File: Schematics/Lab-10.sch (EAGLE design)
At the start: 15 parts, among them IC1 OP350N, Q1 IRLD024

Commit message: Modified changes after prep checkout
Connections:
- removed net N$3: C2.2, IC1.-VS, R6.1
- net +3V3: now also C2.2, IC1.-VS, R6.1
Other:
- note added: "Should be an RC Filter"
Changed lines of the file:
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@@
 <part name="R8" library="EE445L" deviceset="RESISTOR" device="0204/5"/>
 <part name="C2" library="EE445L" deviceset="CAPACITOR" device="025-024X044"/>
+<part name="+3V2" library="EE445L" deviceset="+3V3" device=""/>
 </parts>
 <sheets>
 <sheet>
 <plain>
+<text x="124.46" y="111.76" size="1.778" layer="91">Should be an RC Filter</text>
 </plain>
 <instances>
@@
 <attribute name="VALUE" x="201.549" y="141.224" size="1.778" layer="96" rot="R270"/>
 </instance>
+<instance part="+3V2" gate="G$1" x="205.74" y="154.94" smashed="yes">
+<attribute name="VALUE" x="203.2" y="149.86" size="1.778" layer="96" rot="R90"/>
+</instance>
 </instances>
 <busses>
@@
 <pinref part="+3V1" gate="G$1" pin="+3V3"/>
 </segment>
+<segment>
+<pinref part="IC1" gate="P" pin="-VS"/>
+<wire x1="198.12" y1="162.56" x2="198.12" y2="152.4" width="0.1524" layer="91"/>
+<pinref part="C2" gate="G$1" pin="2"/>
+<wire x1="198.12" y1="152.4" x2="198.12" y2="142.24" width="0.1524" layer="91"/>
+<wire x1="198.12" y1="142.24" x2="200.66" y2="142.24" width="0.1524" layer="91"/>
+<wire x1="198.12" y1="152.4" x2="162.56" y2="152.4" width="0.1524" layer="91"/>
+<junction x="198.12" y="152.4"/>
+<pinref part="R6" gate="G$1" pin="1"/>
+<wire x1="162.56" y1="152.4" x2="162.56" y2="154.94" width="0.1524" layer="91"/>
+<pinref part="+3V2" gate="G$1" pin="+3V3"/>
+<wire x1="198.12" y1="152.4" x2="205.74" y2="152.4" width="0.1524" layer="91"/>
+</segment>
 </net>
 <net name="M0_PWM0" class="0">
@@
 </segment>
 </net>
-<net name="N$3" class="0">
-<segment>
-<pinref part="IC1" gate="P" pin="-VS"/>
-<wire x1="198.12" y1="162.56" x2="198.12" y2="152.4" width="0.1524" layer="91"/>
-<pinref part="C2" gate="G$1" pin="2"/>
-<wire x1="198.12" y1="152.4" x2="198.12" y2="142.24" width="0.1524" layer="91"/>
-<wire x1="198.12" y1="142.24" x2="200.66" y2="142.24" width="0.1524" layer="91"/>
-<wire x1="198.12" y1="152.4" x2="162.56" y2="152.4" width="0.1524" layer="91"/>
-<junction x="198.12" y="152.4"/>
-<pinref part="R6" gate="G$1" pin="1"/>
-<wire x1="162.56" y1="152.4" x2="162.56" y2="154.94" width="0.1524" layer="91"/>
-</segment>
-</net>

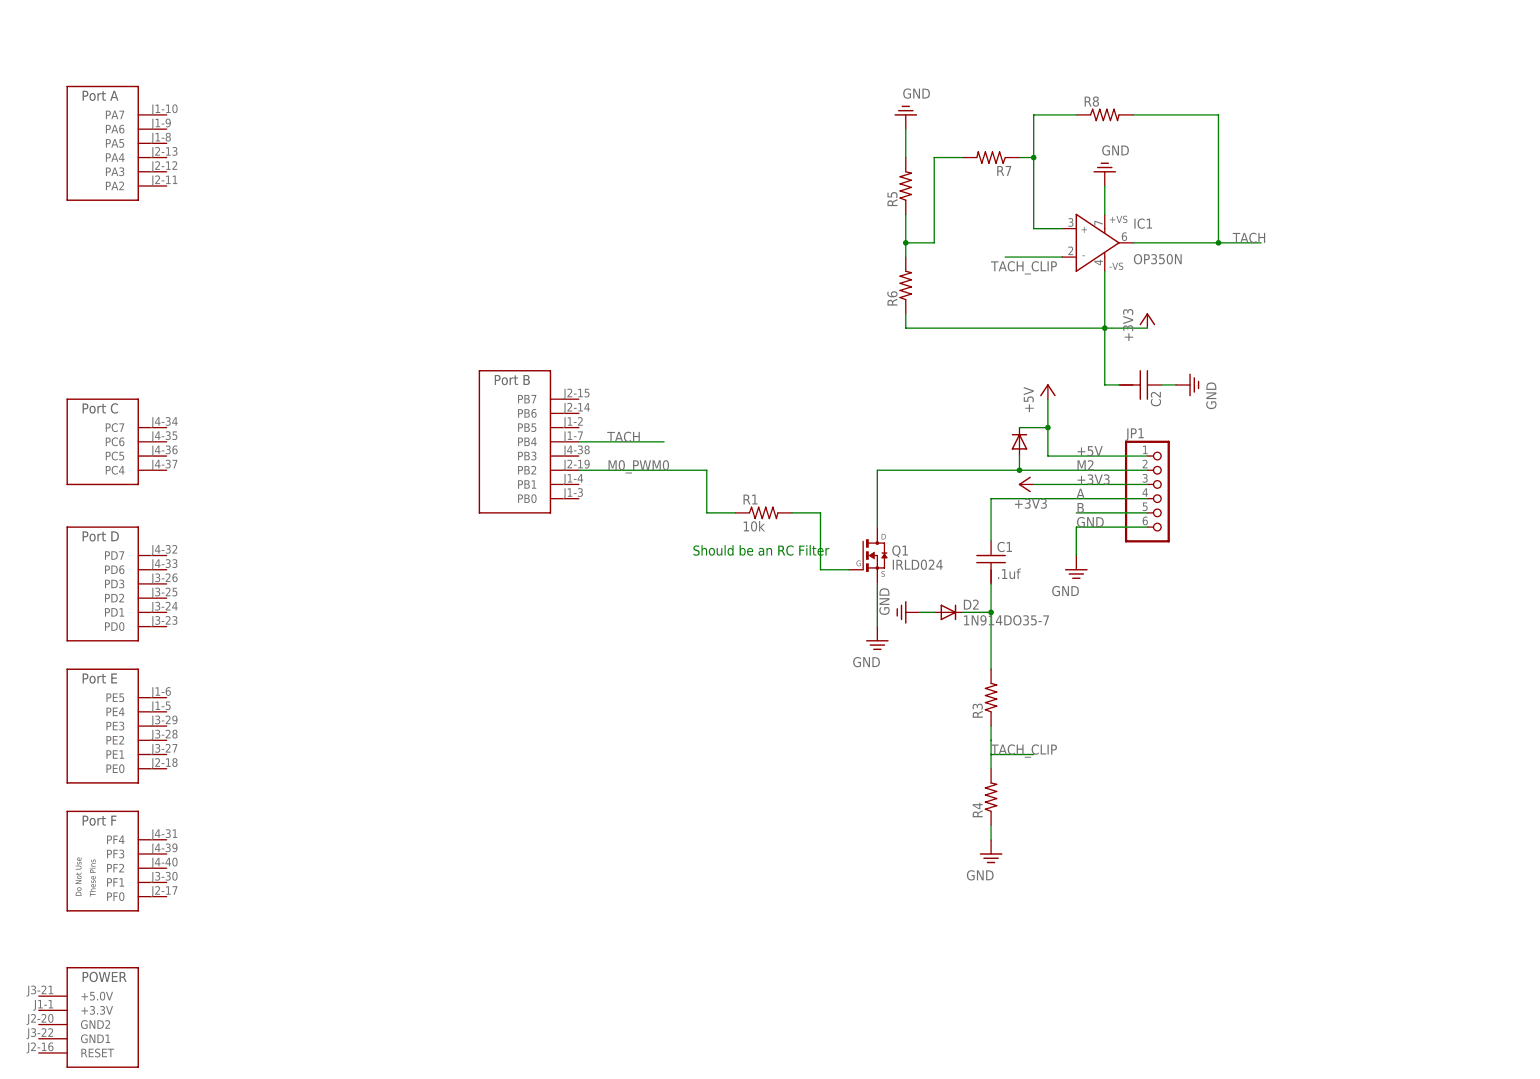
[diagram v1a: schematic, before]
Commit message: Added LCD interface to the schematic
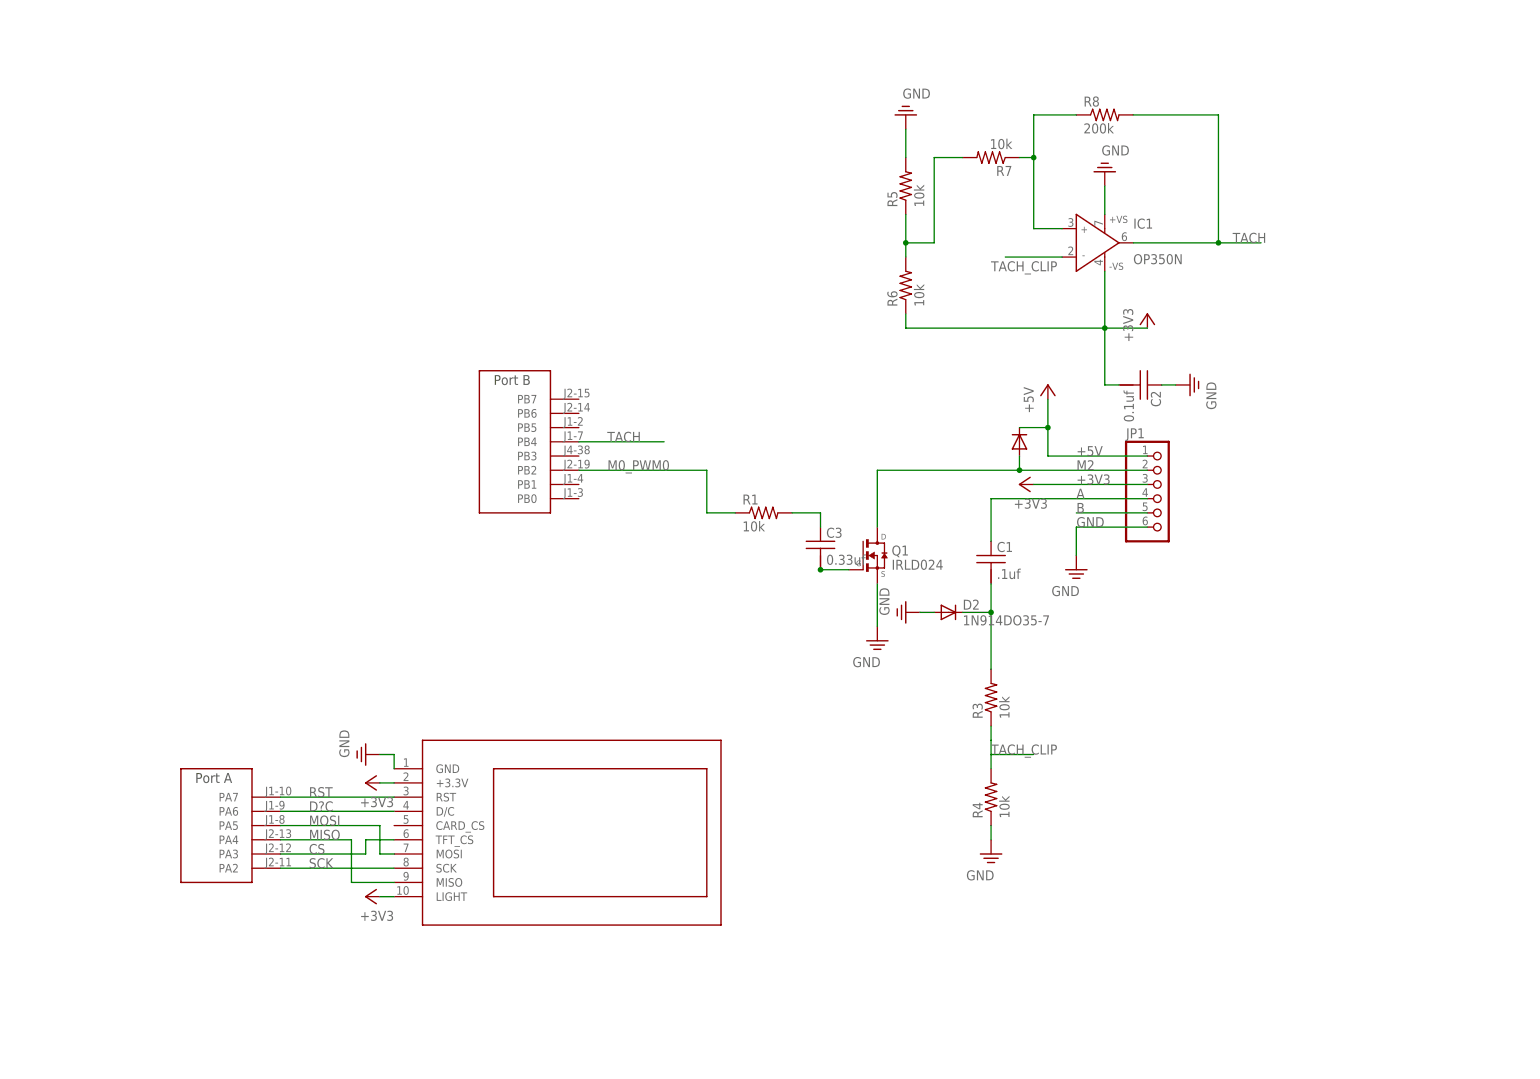
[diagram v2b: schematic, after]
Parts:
- added C3: 0.33uf, EE445L:CAPACITOR025-024X044
- added U$2: ST7735, EE445L:ST7735
- C2: value (none) -> 0.1uf
- R3, R4, R5, R6, R7: value (none) -> 10k
- R8: value (none) -> 200k
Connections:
- new net CS: U$1G$1.PA3, U$2.TFT_CS
- new net D?C: U$1G$1.PA6, U$2.D/C
- new net MISO: U$1G$1.PA4, U$2.MISO
- new net MOSI: U$1G$1.PA5, U$2.MOSI
- new net N$3: C3.2, Q1.G
- new net RST: U$1G$1.PA7, U$2.RST
- new net SCK: U$1G$1.PA2, U$2.SCK
- net +3V3: now also U$2.+3.3V, U$2.LIGHT
- net GND: now also U$2.GND
- net N$1: now also C3.1; no longer Q1.G
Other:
- note removed: "Should be an RC Filter"
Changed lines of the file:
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@@
 <part name="D2" library="EE445L" deviceset="1N914" device="DO35-7"/>
 <part name="SUPPLY3" library="EE445L" deviceset="GND" device=""/>
-<part name="R3" library="EE445L" deviceset="RESISTOR" device="0204/7"/>
-<part name="R4" library="EE445L" deviceset="RESISTOR" device="0204/7"/>
+<part name="R3" library="EE445L" deviceset="RESISTOR" device="0204/7" value="10k"/>
+<part name="R4" library="EE445L" deviceset="RESISTOR" device="0204/7" value="10k"/>
 <part name="SUPPLY4" library="EE445L" deviceset="GND" device=""/>
 <part name="IC1" library="EE445L" deviceset="OP350" device="N"/>
@@
 <part name="SUPPLY6" library="EE445L" deviceset="GND" device=""/>
 <part name="SUPPLY7" library="EE445L" deviceset="GND" device=""/>
-<part name="R5" library="EE445L" deviceset="RESISTOR" device="0204/5"/>
-<part name="R6" library="EE445L" deviceset="RESISTOR" device="0204/5"/>
-<part name="R7" library="EE445L" deviceset="RESISTOR" device="0204/5"/>
-<part name="R8" library="EE445L" deviceset="RESISTOR" device="0204/5"/>
-<part name="C2" library="EE445L" deviceset="CAPACITOR" device="025-024X044"/>
+<part name="R5" library="EE445L" deviceset="RESISTOR" device="0204/5" value="10k"/>
+<part name="R6" library="EE445L" deviceset="RESISTOR" device="0204/5" value="10k"/>
+<part name="R7" library="EE445L" deviceset="RESISTOR" device="0204/5" value="10k"/>
+<part name="R8" library="EE445L" deviceset="RESISTOR" device="0204/5" value="200k"/>
+<part name="C2" library="EE445L" deviceset="CAPACITOR" device="025-024X044" value="0.1uf"/>
 <part name="+3V2" library="EE445L" deviceset="+3V3" device=""/>
+<part name="C3" library="EE445L" deviceset="CAPACITOR" device="025-024X044" value="0.33uf"/>
+<part name="U$2" library="EE445L" deviceset="ST7735" device=""/>
+<part name="+3V3" library="EE445L" deviceset="+3V3" device=""/>
+<part name="+3V4" library="EE445L" deviceset="+3V3" device=""/>
+<part name="SUPPLY8" library="EE445L" deviceset="GND" device=""/>
 </parts>
 <sheets>
 <sheet>
 <plain>
-<text x="124.46" y="111.76" size="1.778" layer="91">Should be an RC Filter</text>
 </plain>
 <instances>
@@
 <attribute name="DRAWING_NAME" x="190.5" y="19.05" size="2.54" layer="94"/>
 </instance>
-<instance part="U$1" gate="G$1" x="12.7" y="175.26" smashed="yes"/>
+<instance part="U$1" gate="G$1" x="33.02" y="53.34" smashed="yes"/>
 <instance part="U$1" gate="G$2" x="86.36" y="119.38" smashed="yes"/>
-<instance part="U$1" gate="G$3" x="12.7" y="124.46" smashed="yes"/>
-<instance part="U$1" gate="G$4" x="12.7" y="96.52" smashed="yes"/>
-<instance part="U$1" gate="G$5" x="12.7" y="71.12" smashed="yes"/>
-<instance part="U$1" gate="G$6" x="12.7" y="48.26" smashed="yes"/>
-<instance part="U$1" gate="G$7" x="12.7" y="20.32" smashed="yes"/>
 <instance part="D2" gate="G$1" x="170.18" y="101.6" smashed="yes">
 <attribute name="NAME" x="172.72" y="102.0826" size="1.778" layer="95"/>
@@
 <instance part="+3V2" gate="G$1" x="205.74" y="154.94" smashed="yes">
 <attribute name="VALUE" x="203.2" y="149.86" size="1.778" layer="96" rot="R90"/>
+</instance>
+<instance part="C3" gate="G$1" x="147.32" y="114.3" smashed="yes">
+<attribute name="NAME" x="148.336" y="114.935" size="1.778" layer="95"/>
+<attribute name="VALUE" x="148.336" y="110.109" size="1.778" layer="96"/>
+</instance>
+<instance part="U$2" gate="G$1" x="76.2" y="45.72" smashed="yes"/>
+<instance part="+3V3" gate="G$1" x="66.04" y="71.12" smashed="yes" rot="R90">
+<attribute name="VALUE" x="71.12" y="68.58" size="1.778" layer="96" rot="R180"/>
+</instance>
+<instance part="+3V4" gate="G$1" x="66.04" y="50.8" smashed="yes" rot="R90">
+<attribute name="VALUE" x="71.12" y="48.26" size="1.778" layer="96" rot="R180"/>
+</instance>
+<instance part="SUPPLY8" gate="GND" x="66.04" y="76.2" smashed="yes" rot="R270">
+<attribute name="VALUE" x="61.341" y="80.645" size="1.778" layer="96" rot="R270"/>
 </instance>
 </instances>
@@
 <pinref part="SUPPLY7" gate="GND" pin="GND"/>
 <wire x1="162.56" y1="182.88" x2="162.56" y2="187.96" width="0.1524" layer="91"/>
+</segment>
+<segment>
+<pinref part="SUPPLY8" gate="GND" pin="GND"/>
+<pinref part="U$2" gate="G$1" pin="GND"/>
+<wire x1="68.58" y1="76.2" x2="71.12" y2="76.2" width="0.1524" layer="91"/>
+<wire x1="71.12" y1="76.2" x2="71.12" y2="73.66" width="0.1524" layer="91"/>
 </segment>
 </net>
@@
 <wire x1="198.12" y1="152.4" x2="205.74" y2="152.4" width="0.1524" layer="91"/>
 </segment>
+<segment>
+<pinref part="+3V3" gate="G$1" pin="+3V3"/>
+<pinref part="U$2" gate="G$1" pin="+3.3V"/>
+<wire x1="68.58" y1="71.12" x2="71.12" y2="71.12" width="0.1524" layer="91"/>
+</segment>
+<segment>
+<pinref part="U$2" gate="G$1" pin="LIGHT"/>
+<pinref part="+3V4" gate="G$1" pin="+3V3"/>
+<wire x1="71.12" y1="50.8" x2="68.58" y2="50.8" width="0.1524" layer="91"/>
+</segment>
 </net>
 <net name="M0_PWM0" class="0">
@@
 <pinref part="R1" gate="G$1" pin="2"/>
 <wire x1="142.24" y1="119.38" x2="147.32" y2="119.38" width="0.1524" layer="91"/>
-<wire x1="147.32" y1="119.38" x2="147.32" y2="109.22" width="0.1524" layer="91"/>
-<pinref part="Q1" gate="G$1" pin="G"/>
-<wire x1="147.32" y1="109.22" x2="152.4" y2="109.22" width="0.1524" layer="91"/>
+<pinref part="C3" gate="G$1" pin="1"/>
+<wire x1="147.32" y1="119.38" x2="147.32" y2="116.84" width="0.1524" layer="91"/>
 </segment>
 </net>
@@
 </segment>
 </net>
+<net name="N$3" class="0">
+<segment>
+<pinref part="Q1" gate="G$1" pin="G"/>
+<pinref part="C3" gate="G$1" pin="2"/>
+<junction x="147.32" y="109.22"/>
+<wire x1="147.32" y1="109.22" x2="152.4" y2="109.22" width="0.1524" layer="91"/>
+</segment>
+</net>
+<net name="RST" class="0">
+<segment>
+<pinref part="U$1" gate="G$1" pin="PA7"/>
+<pinref part="U$2" gate="G$1" pin="RST"/>
+<wire x1="50.8" y1="68.58" x2="71.12" y2="68.58" width="0.1524" layer="91"/>
+<label x="55.88" y="68.58" size="1.778" layer="95"/>
+</segment>
+</net>
+<net name="D?C" class="0">
+<segment>
+<pinref part="U$1" gate="G$1" pin="PA6"/>
+<pinref part="U$2" gate="G$1" pin="D/C"/>
+<wire x1="50.8" y1="66.04" x2="71.12" y2="66.04" width="0.1524" layer="91"/>
+<label x="55.88" y="66.04" size="1.778" layer="95"/>
+</segment>
+</net>
+<net name="MOSI" class="0">
+<segment>
+<pinref part="U$1" gate="G$1" pin="PA5"/>
+<wire x1="50.8" y1="63.5" x2="68.58" y2="63.5" width="0.1524" layer="91"/>
+<pinref part="U$2" gate="G$1" pin="MOSI"/>
+<wire x1="68.58" y1="63.5" x2="68.58" y2="58.42" width="0.1524" layer="91"/>
+<wire x1="68.58" y1="58.42" x2="71.12" y2="58.42" width="0.1524" layer="91"/>
+<label x="55.88" y="63.5" size="1.778" layer="95"/>
+</segment>
+</net>
+<net name="MISO" class="0">
+<segment>
+<pinref part="U$1" gate="G$1" pin="PA4"/>
+<wire x1="50.8" y1="60.96" x2="63.5" y2="60.96" width="0.1524" layer="91"/>
+<pinref part="U$2" gate="G$1" pin="MISO"/>
+<wire x1="63.5" y1="60.96" x2="63.5" y2="53.34" width="0.1524" layer="91"/>
+<wire x1="63.5" y1="53.34" x2="71.12" y2="53.34" width="0.1524" layer="91"/>
+<label x="55.88" y="60.96" size="1.778" layer="95"/>
+</segment>
+</net>
+<net name="CS" class="0">
+<segment>
+<pinref part="U$1" gate="G$1" pin="PA3"/>
+<wire x1="50.8" y1="58.42" x2="66.04" y2="58.42" width="0.1524" layer="91"/>
+<pinref part="U$2" gate="G$1" pin="TFT_CS"/>
+<wire x1="66.04" y1="58.42" x2="66.04" y2="60.96" width="0.1524" layer="91"/>
+<wire x1="66.04" y1="60.96" x2="71.12" y2="60.96" width="0.1524" layer="91"/>
+<label x="55.88" y="58.42" size="1.778" layer="95"/>
+</segment>
+</net>
+<net name="SCK" class="0">
+<segment>
+<pinref part="U$1" gate="G$1" pin="PA2"/>
+<pinref part="U$2" gate="G$1" pin="SCK"/>
+<wire x1="50.8" y1="55.88" x2="71.12" y2="55.88" width="0.1524" layer="91"/>
+<label x="55.88" y="55.88" size="1.778" layer="95"/>
+</segment>
+</net>

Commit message: Added wifi block
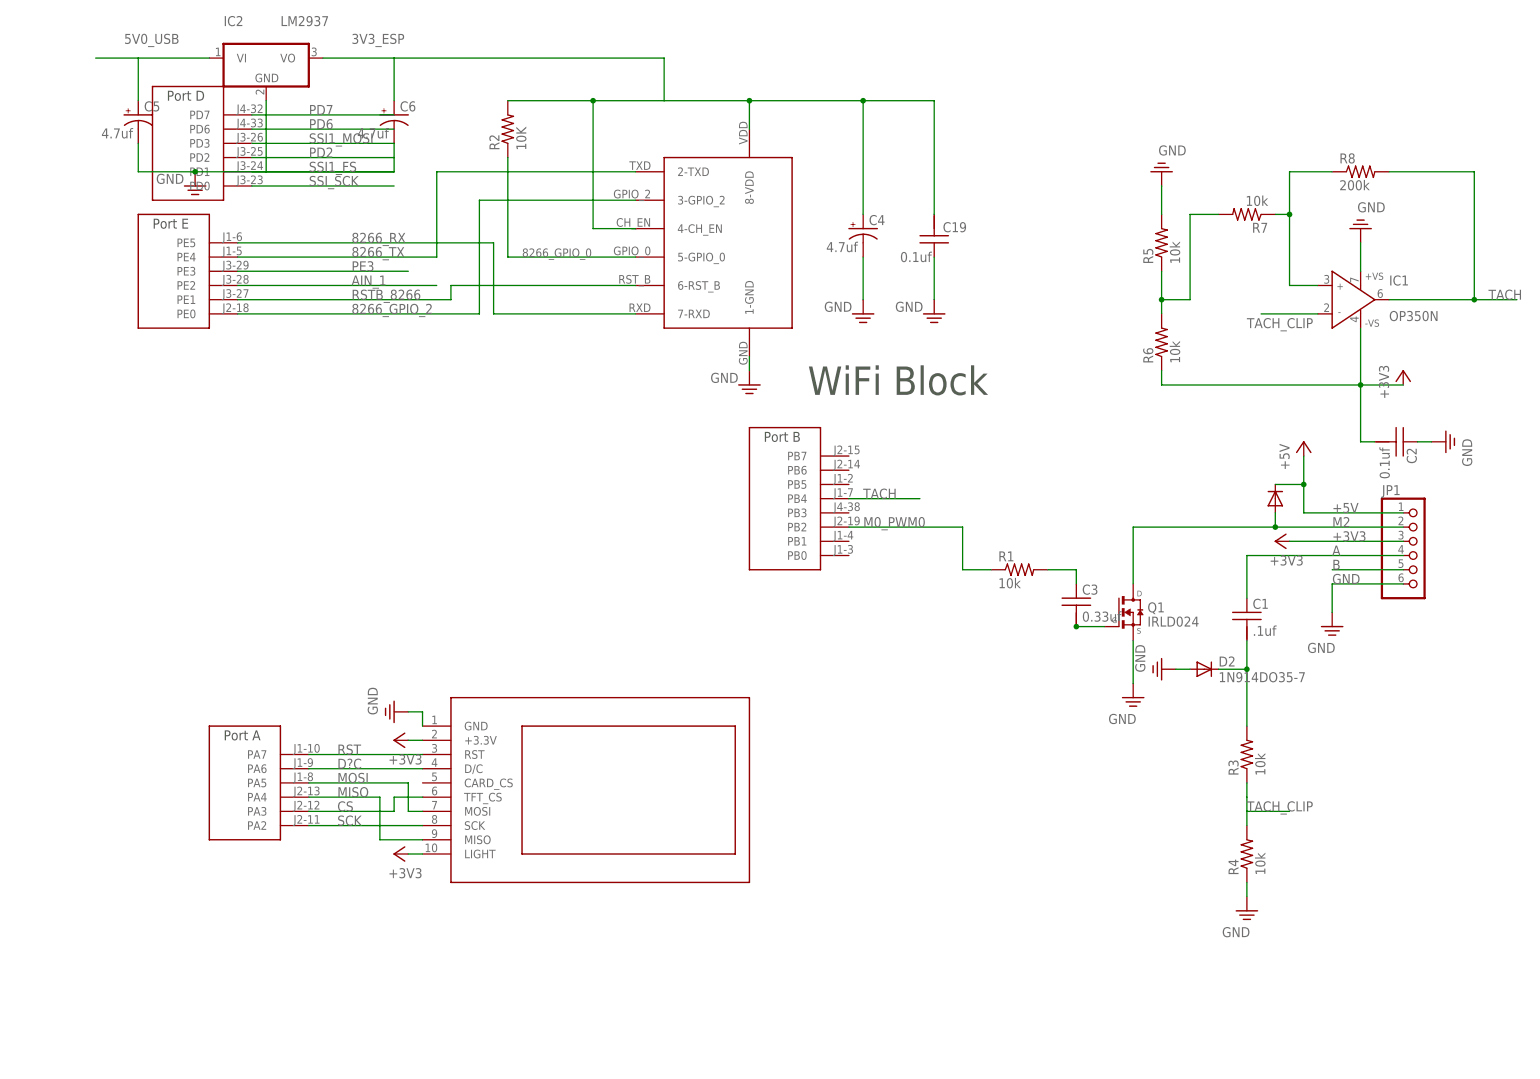
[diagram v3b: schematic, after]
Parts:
- added C19: 0.1uf, EE445L:CAPACITOR050-024X044
- added C4, C5, C6: 4.7uf, EE445L:CAPACITOR_POLARIZEDE5-6
- added IC2: LM2937, linear:LM2937
- added R2: 10K, EE445L:RESISTOR0204/7
- added U$3: ESP_8266, EE445L:ESP_8266
- added U$4, U$5: TM4C_BP, EE445L:TM4C_BP
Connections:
- new net 3V3_ESP: C19.2, C4.+, C6.+, IC2.VO, R2.2, U$3.4-CH_EN, U$3.8-VDD
- new net 5V0_USB: C5.+, IC2.VI
- new net 8266_GPIO_0: R2.1, U$3.5-GPIO_0
- new net 8266_GPIO_2: U$3.3-GPIO_2, U$4G$5.PE0
- new net 8266_RX: U$3.7-RXD, U$4G$5.PE5
- new net 8266_TX: U$3.2-TXD, U$4G$5.PE4
- new net AIN_1: U$4G$5.PE2
- new net PD2: U$5G$4.PD2
- new net PD6: U$5G$4.PD6
- new net PD7: U$5G$4.PD7
- new net PE3: U$4G$5.PE3
- new net RSTB_8266: U$3.6-RST_B, U$4G$5.PE1
- new net SSI1_FS: U$5G$4.PD1
- new net SSI1_MOSI: U$5G$4.PD3
- new net SSI_SCK: U$5G$4.PD0
- net GND: now also C19.1, C4.-, C5.-, C6.-, IC2.GND, U$3.1-GND
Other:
- note added: "WiFi Block"
- moved on the sheet: C1, C2, C3, D2, IC1, JP1, Q1, R1, R3, R4, R5, R6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
